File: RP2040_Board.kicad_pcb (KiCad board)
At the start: 2 copper layers, 60 parts, among them J10 24V DC Power, J2 mA_OUT, J7 mA_IN, J9 GND-24V, Q1 IRF510N, Q2 BC337, Q3 BC337, U1 Pico, U2 LM324, U3 PC817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

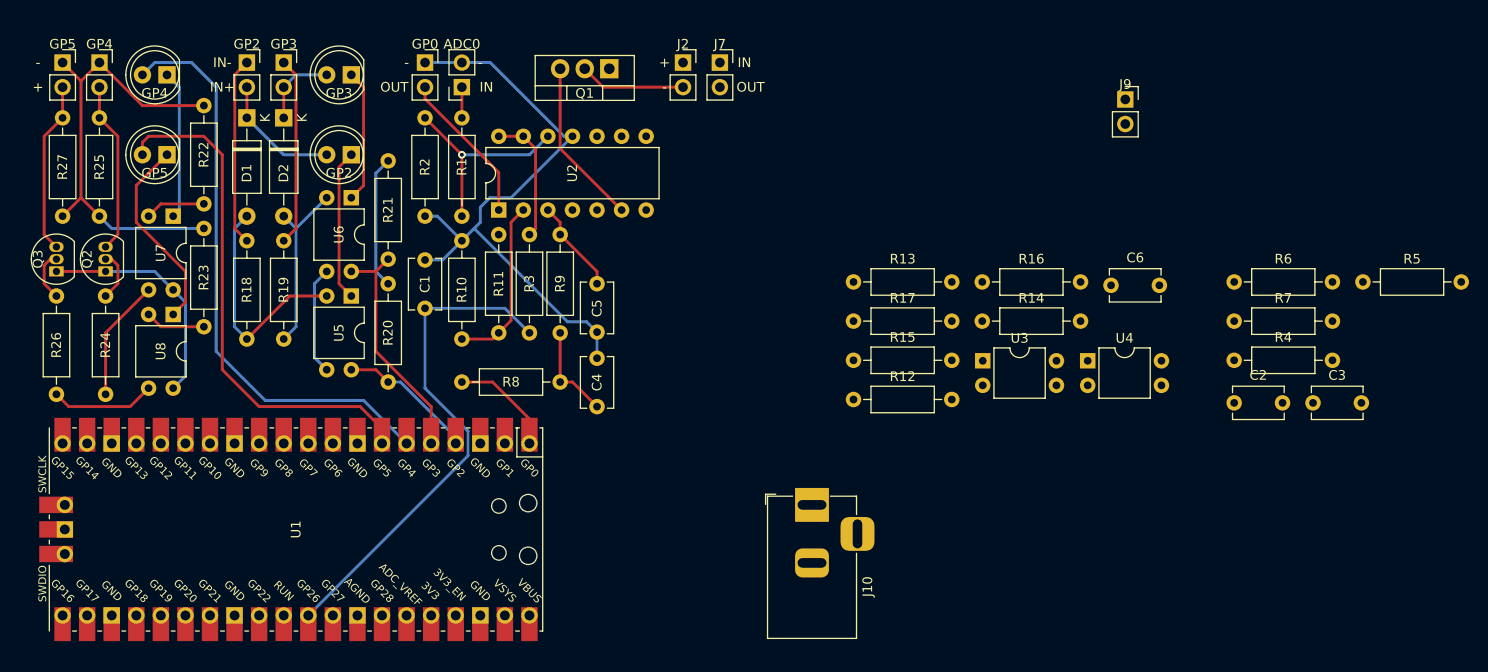
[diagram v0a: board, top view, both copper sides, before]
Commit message: Added a copper pad for ground
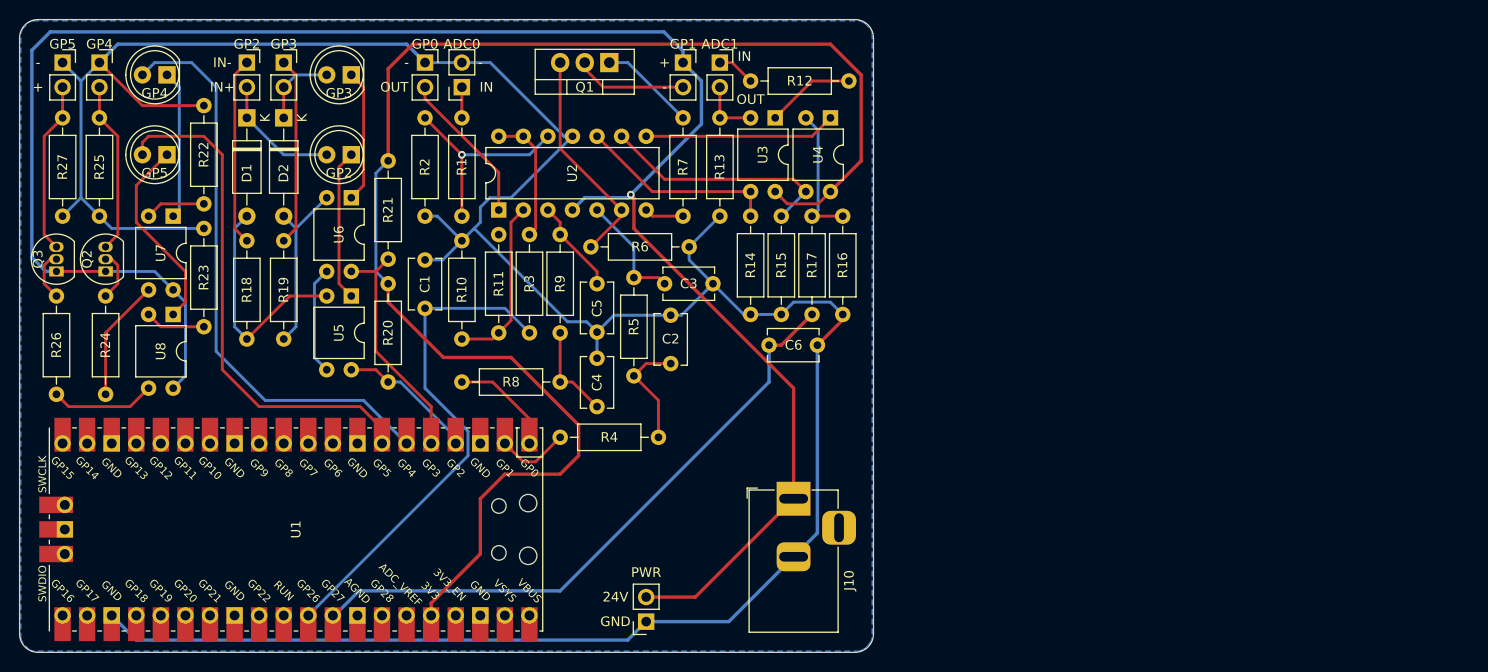
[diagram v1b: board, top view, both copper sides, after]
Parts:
- removed J9: GND-24V, Connector_PinSocket_2.54mm:PinSocket_1x02_P2.54mm_Vertical
- added PWR: GND-24V, Connector_PinSocket_2.54mm:PinSocket_1x02_P2.54mm_Vertical, F.Cu at (139.1, 132.7)
- moved R5 75.4 mm to (137.8, 97.2), turned to 270 degrees
- moved C3 68.1 mm to (141.0, 97.8)
- moved R6 66.6 mm to (133.3, 94.0)
- moved R7 60.7 mm to (142.9, 80.6), turned to 270 degrees
- moved R4 60.0 mm to (140.3, 113.7), turned to 180 degrees
- moved C2 58.4 mm to (141.6, 106.0), turned to 90 degrees
- moved U4 36.6 mm to (158.1, 80.6), turned to 270 degrees
- moved C6 35.9 mm to (151.8, 104.1)
- moved U3 33.0 mm to (152.4, 80.6), turned to 270 degrees
- moved R12 32.9 mm to (160.0, 76.8), turned to 180 degrees
- moved R14 24.0 mm to (149.9, 101.0), turned to 90 degrees
- moved R13 15.4 mm to (146.7, 90.8), turned to 90 degrees
- moved R16 14.8 mm to (159.4, 101.0), turned to 90 degrees
- moved R15 8.84 mm to (153.0, 101.0), turned to 90 degrees
- moved R17 4.34 mm to (156.2, 101.0), turned to 90 degrees
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- renumbered J7 to ADC1, J2 to GP1
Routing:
- net 24V: track 24.1 -> 200.7 mm, vias 0 -> 1
- net GND: track 122.5 -> 299.2 mm
- net 3.3V: track 13.8 -> 150.9 mm
- net /20mA to 3.3V Input/OUT: track 0.00 -> 65.5 mm
- net Net-(R15-Pad2): track 0.00 -> 25.0 mm
- net Net-(R14-Pad2): track 0.00 -> 20.8 mm
- net Net-(U2-Pad8): track 0.00 -> 19.8 mm
- net Net-(R16-Pad2): track 0.00 -> 14.1 mm
- net Net-(C3-Pad1): track 0.00 -> 12.0 mm
- net Net-(C2-Pad1): track 0.00 -> 11.7 mm
- net Net-(Q1-Pad1): track 0.00 -> 9.99 mm
- net Net-(R12-Pad1): track 0.00 -> 9.20 mm
- net /PWM to 20mA Output/PWM: track 0.00 -> 7.56 mm
- net /20mA to 3.3V Input/C_OUT: track 0.00 -> 6.35 mm
- net Net-(Q1-Pad3): track 17.2 -> 22.4 mm
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- added copper zone on B.Cu, net GND
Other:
- board outline added: 88.3 x 65.4 mm
- board text added: "24V"
- board text added: "GND"

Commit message: Forgot to add a small trace. Now the board is complete.
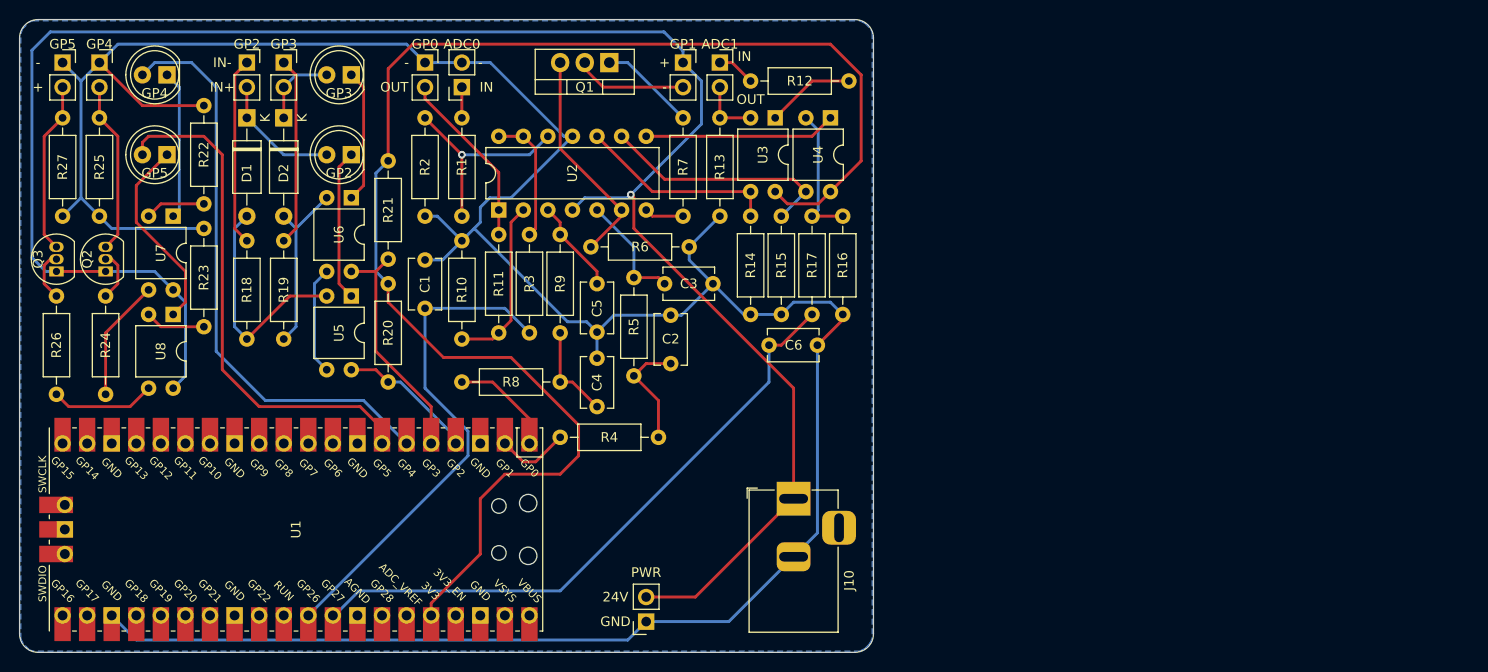
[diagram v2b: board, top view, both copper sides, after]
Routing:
- net /PWM to 10V Output/OUT: track 15.9 -> 18.4 mm

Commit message: Adjusted 24V traces to be .35mm and recreated fill zone
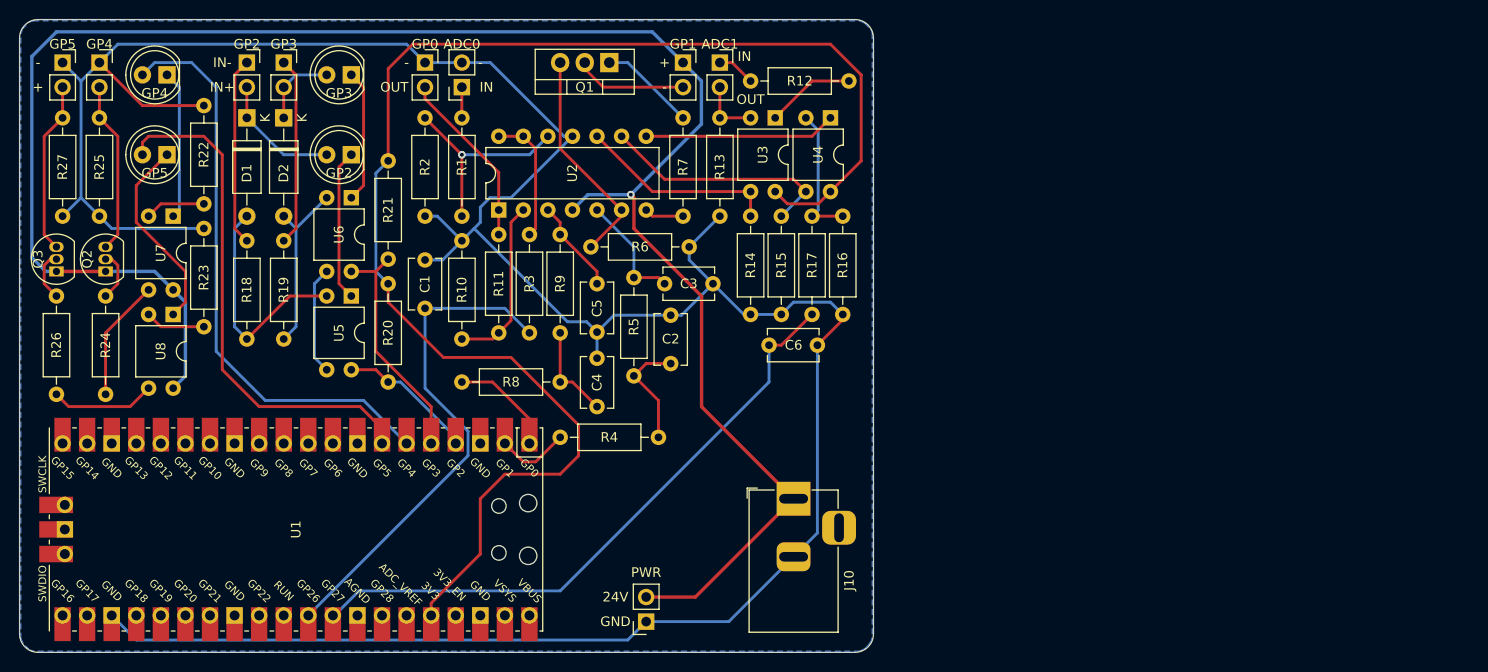
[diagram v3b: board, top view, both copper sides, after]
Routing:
- net 24V: track 200.7 -> 199.7 mm
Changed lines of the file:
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@@
     (thickness 1.6)
     (drawings 22)
-    (tracks 275)
+    (tracks 274)
     (zones 0)
     (modules 60)
@@
   (segment (start 134.62 77.47) (end 142.875 77.47) (width 0.3) (layer F.Cu) (net 19))
   (segment (start 132.715 75.565) (end 134.62 77.47) (width 0.3) (layer F.Cu) (net 19))
-  (segment (start 78.105 96.52) (end 83.185 96.52) (width 0.3) (layer F.Cu) (net 20))
-  (segment (start 91.44 99.695) (end 90.17 98.425) (width 0.3) (layer B.Cu) (net 20))
-  (segment (start 91.44 107.315) (end 91.44 99.695) (width 0.3) (layer B.Cu) (net 20))
-  (segment (start 90.17 108.585) (end 91.44 107.315) (width 0.3) (layer B.Cu) (net 20))
-  (segment (start 88.265 96.52) (end 83.185 96.52) (width 0.3) (layer B.Cu) (net 20))
-  (segment (start 90.17 98.425) (end 88.265 96.52) (width 0.3) (layer B.Cu) (net 20))
-  (segment (start 144.145 130.175) (end 154.305 120.015) (width 0.3) (layer F.Cu) (net 20))
-  (segment (start 139.065 130.175) (end 144.145 130.175) (width 0.3) (layer F.Cu) (net 20))
-  (segment (start 144.78 81.28) (end 144.78 76.835) (width 0.3) (layer B.Cu) (net 20))
-  (segment (start 144.78 76.835) (end 142.875 74.93) (width 0.3) (layer B.Cu) (net 20))
-  (segment (start 137.16 88.9) (end 137.4775 88.5825) (width 0.3) (layer B.Cu) (net 20))
-  (segment (start 132.715 88.9) (end 137.16 88.9) (width 0.3) (layer B.Cu) (net 20))
-  (segment (start 131.445 90.17) (end 132.715 88.9) (width 0.3) (layer B.Cu) (net 20))
-  (segment (start 137.4775 88.5825) (end 144.78 81.28) (width 0.3) (layer B.Cu) (net 20))
+  (segment (start 78.105 96.52) (end 83.185 96.52) (width 0.35) (layer F.Cu) (net 20))
+  (segment (start 88.265 96.52) (end 83.185 96.52) (width 0.35) (layer B.Cu) (net 20))
+  (segment (start 90.17 98.425) (end 88.265 96.52) (width 0.35) (layer B.Cu) (net 20))
+  (segment (start 144.145 130.175) (end 154.305 120.015) (width 0.35) (layer F.Cu) (net 20))
+  (segment (start 139.065 130.175) (end 144.145 130.175) (width 0.35) (layer F.Cu) (net 20))
   (via (at 137.4775 88.5825) (size 0.8) (drill 0.4) (layers F.Cu B.Cu) (net 20))
-  (segment (start 137.4775 88.5825) (end 137.795 88.9) (width 0.3) (layer F.Cu) (net 20))
-  (segment (start 137.795 88.9) (end 137.795 92.075) (width 0.3) (layer F.Cu) (net 20))
-  (segment (start 154.305 108.585) (end 154.305 120.015) (width 0.3) (layer F.Cu) (net 20))
-  (segment (start 137.795 92.075) (end 154.305 108.585) (width 0.3) (layer F.Cu) (net 20))
-  (segment (start 142.875 73.73) (end 140.9 71.755) (width 0.3) (layer B.Cu) (net 20))
-  (segment (start 142.875 74.93) (end 142.875 73.73) (width 0.3) (layer B.Cu) (net 20))
-  (segment (start 140.9 71.755) (end 77.47 71.755) (width 0.3) (layer B.Cu) (net 20))
-  (segment (start 77.47 71.755) (end 75.565 73.66) (width 0.3) (layer B.Cu) (net 20))
-  (segment (start 77.005 96.52) (end 78.105 96.52) (width 0.3) (layer B.Cu) (net 20))
-  (segment (start 75.565 95.08) (end 77.005 96.52) (width 0.3) (layer B.Cu) (net 20))
-  (segment (start 75.565 73.66) (end 75.565 95.08) (width 0.3) (layer B.Cu) (net 20))
+  (segment (start 144.794999 110.504999) (end 144.794999 99.074999) (width 0.35) (layer F.Cu) (net 20))
+  (segment (start 154.305 120.015) (end 144.794999 110.504999) (width 0.35) (layer F.Cu) (net 20))
+  (segment (start 144.794999 99.074999) (end 137.795 92.075) (width 0.35) (layer F.Cu) (net 20))
+  (segment (start 137.795 88.9) (end 137.4775 88.5825) (width 0.35) (layer F.Cu) (net 20))
+  (segment (start 137.795 92.075) (end 137.795 88.9) (width 0.35) (layer F.Cu) (net 20))
+  (segment (start 133.0325 88.5825) (end 131.445 90.17) (width 0.35) (layer B.Cu) (net 20))
+  (segment (start 137.4775 88.5825) (end 133.0325 88.5825) (width 0.35) (layer B.Cu) (net 20))
+  (segment (start 137.4775 88.5825) (end 144.78 81.28) (width 0.35) (layer B.Cu) (net 20))
+  (segment (start 144.78 76.835) (end 142.875 74.93) (width 0.35) (layer B.Cu) (net 20))
+  (segment (start 144.78 81.28) (end 144.78 76.835) (width 0.35) (layer B.Cu) (net 20))
+  (segment (start 139.7 71.755) (end 142.875 74.93) (width 0.35) (layer B.Cu) (net 20))
+  (segment (start 78.105 71.755) (end 139.7 71.755) (width 0.35) (layer B.Cu) (net 20))
+  (segment (start 75.565 74.295) (end 78.105 71.755) (width 0.35) (layer B.Cu) (net 20))
+  (segment (start 75.565 95.08) (end 75.565 74.295) (width 0.35) (layer B.Cu) (net 20))
+  (segment (start 77.005 96.52) (end 75.565 95.08) (width 0.35) (layer B.Cu) (net 20))
+  (segment (start 78.105 96.52) (end 77.005 96.52) (width 0.35) (layer B.Cu) (net 20))
+  (segment (start 90.17 98.425) (end 91.44 99.695) (width 0.35) (layer B.Cu) (net 20))
+  (segment (start 91.44 107.315) (end 90.17 108.585) (width 0.35) (layer B.Cu) (net 20))
+  (segment (start 91.44 99.695) (end 91.44 107.315) (width 0.35) (layer B.Cu) (net 20))
   (segment (start 96.539999 92.094999) (end 97.79 93.345) (width 0.3) (layer F.Cu) (net 21))
   (segment (start 96.539999 76.180001) (end 96.539999 92.094999) (width 0.3) (layer F.Cu) (net 21))
